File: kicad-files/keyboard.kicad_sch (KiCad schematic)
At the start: 163 parts, among them J1 TYPE-C-31-M12_13, U1 STM32F411CEU6, U2 USBLC6-2SC6, U3 AT24C256C-SSHL-T, U4 SGM2007-3.3XN5/TR, Y1 TAXM8M4RFDCET2T

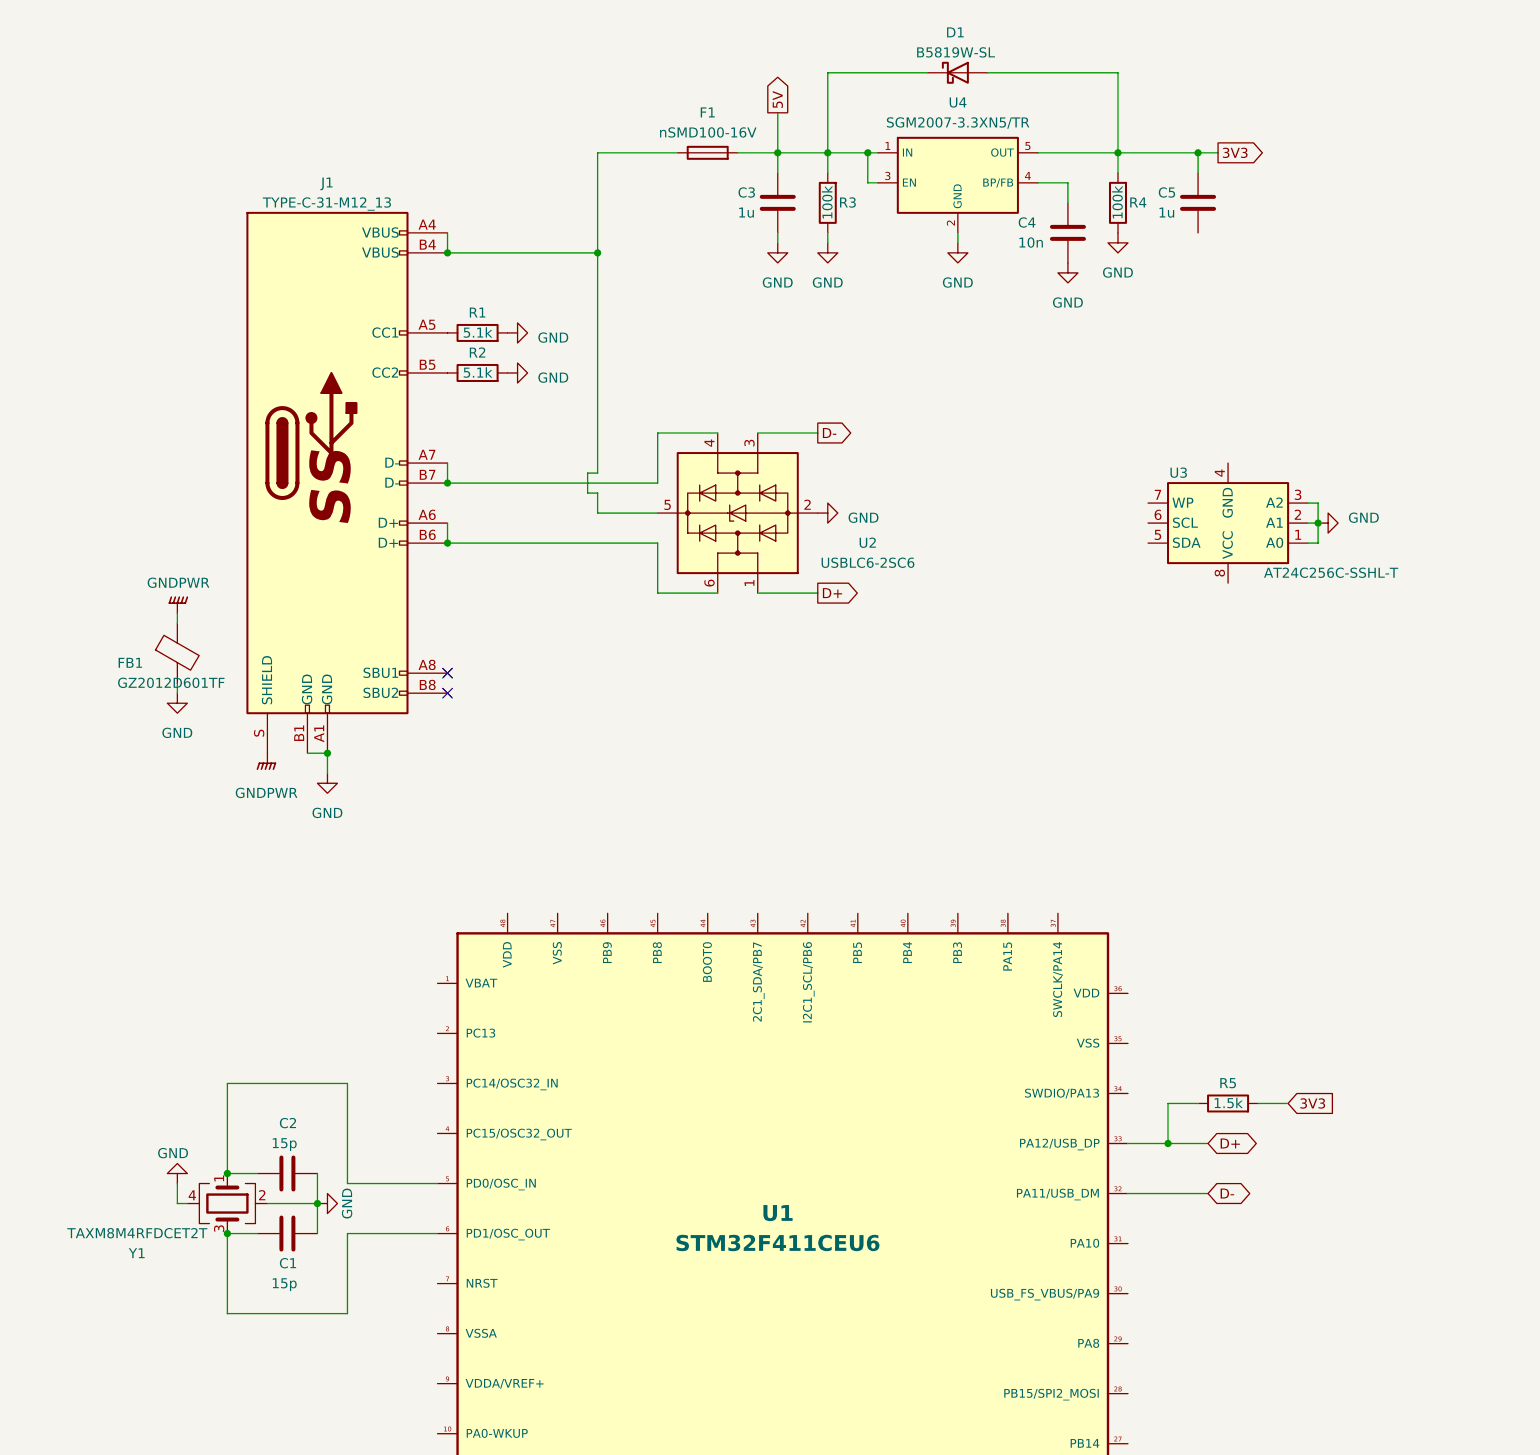
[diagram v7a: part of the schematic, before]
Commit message: Connected EEPROM to STM
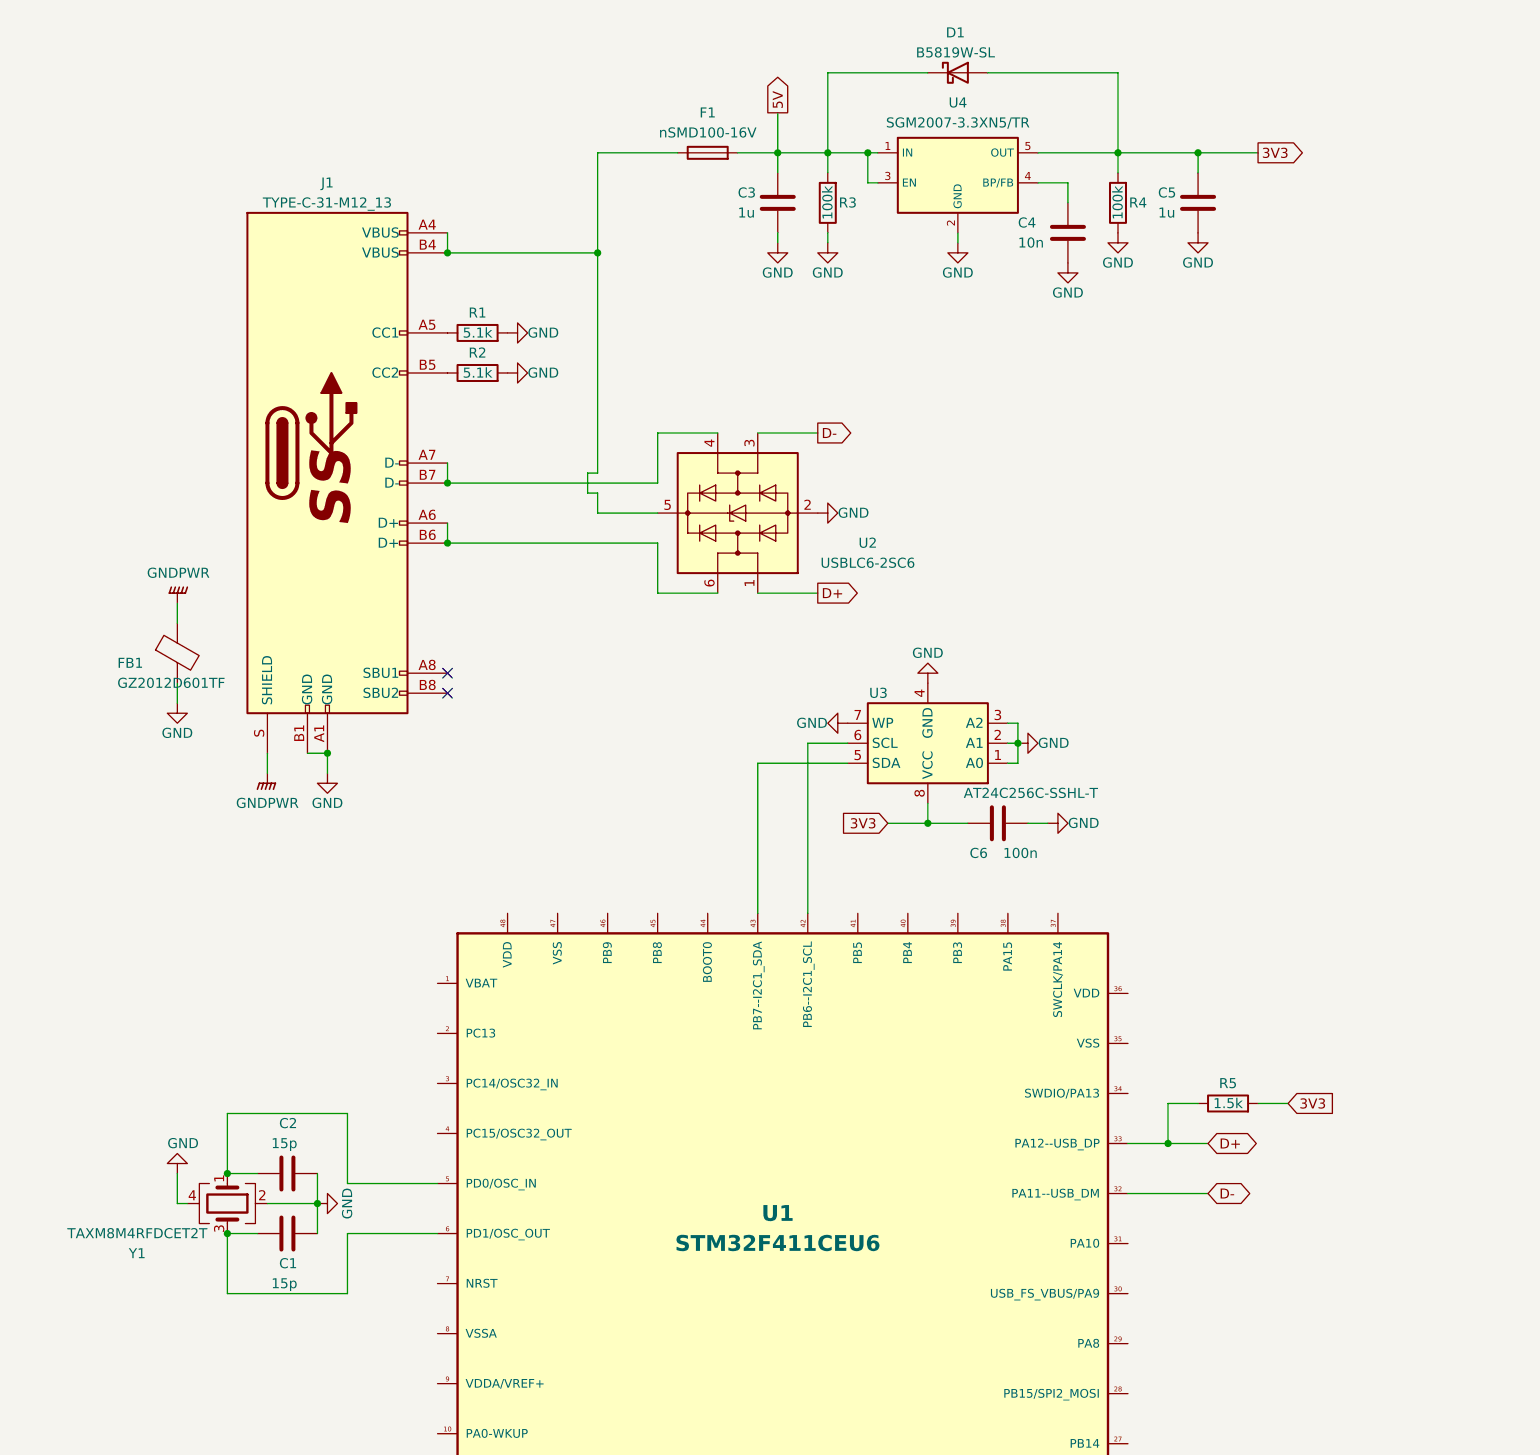
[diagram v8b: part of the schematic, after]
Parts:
- added C6: 100n, Capacitor_SMD:C_0603_1608Metric_Pad1.08x0.95mm_HandSolder, symbol Device:C
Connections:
- net 3V3: now also U3.8 (VCC), C6.1
- net GND: now also C5.2, U3.4 (GND), U3.7 (WP), C6.2
- net at U3.5 (SDA): now also U1.43 (PB7--I2C1_SDA)
- net at U3.6 (SCL): now also U1.42 (PB6--I2C1_SCL)
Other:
- moved on the sheet: U3
